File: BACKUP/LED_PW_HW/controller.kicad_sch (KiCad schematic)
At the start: 23 parts, among them SW1 SW_MEC_5E, U2 STM32L031K6Tx, Y1 Crystal

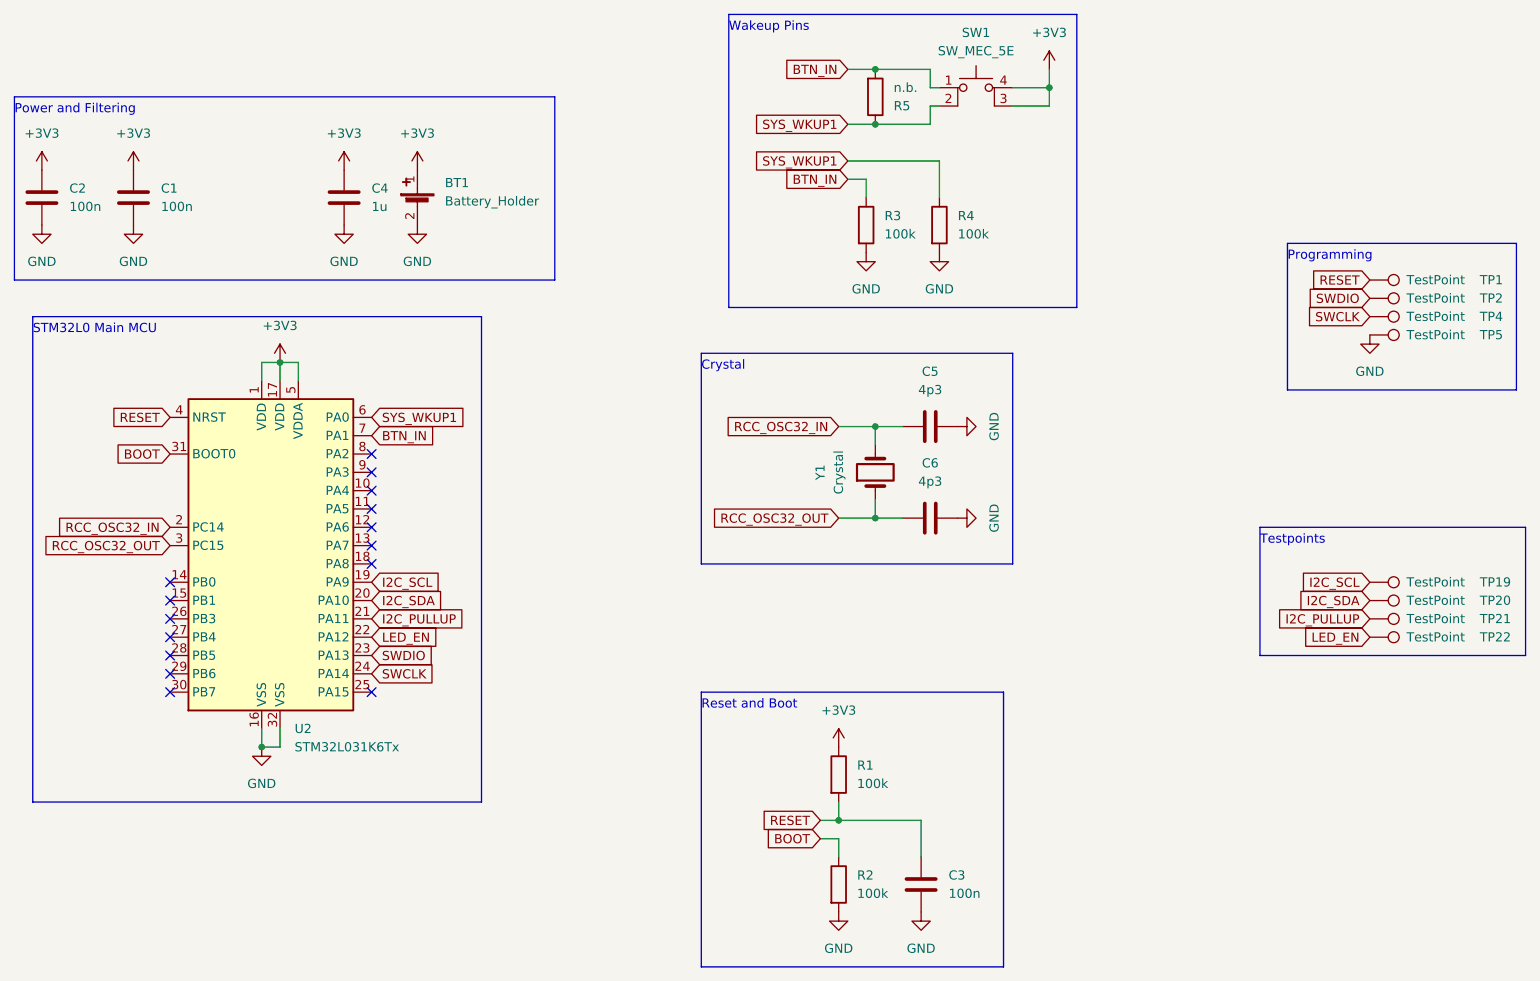
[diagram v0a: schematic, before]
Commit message: giving up for now and going with 72 leds
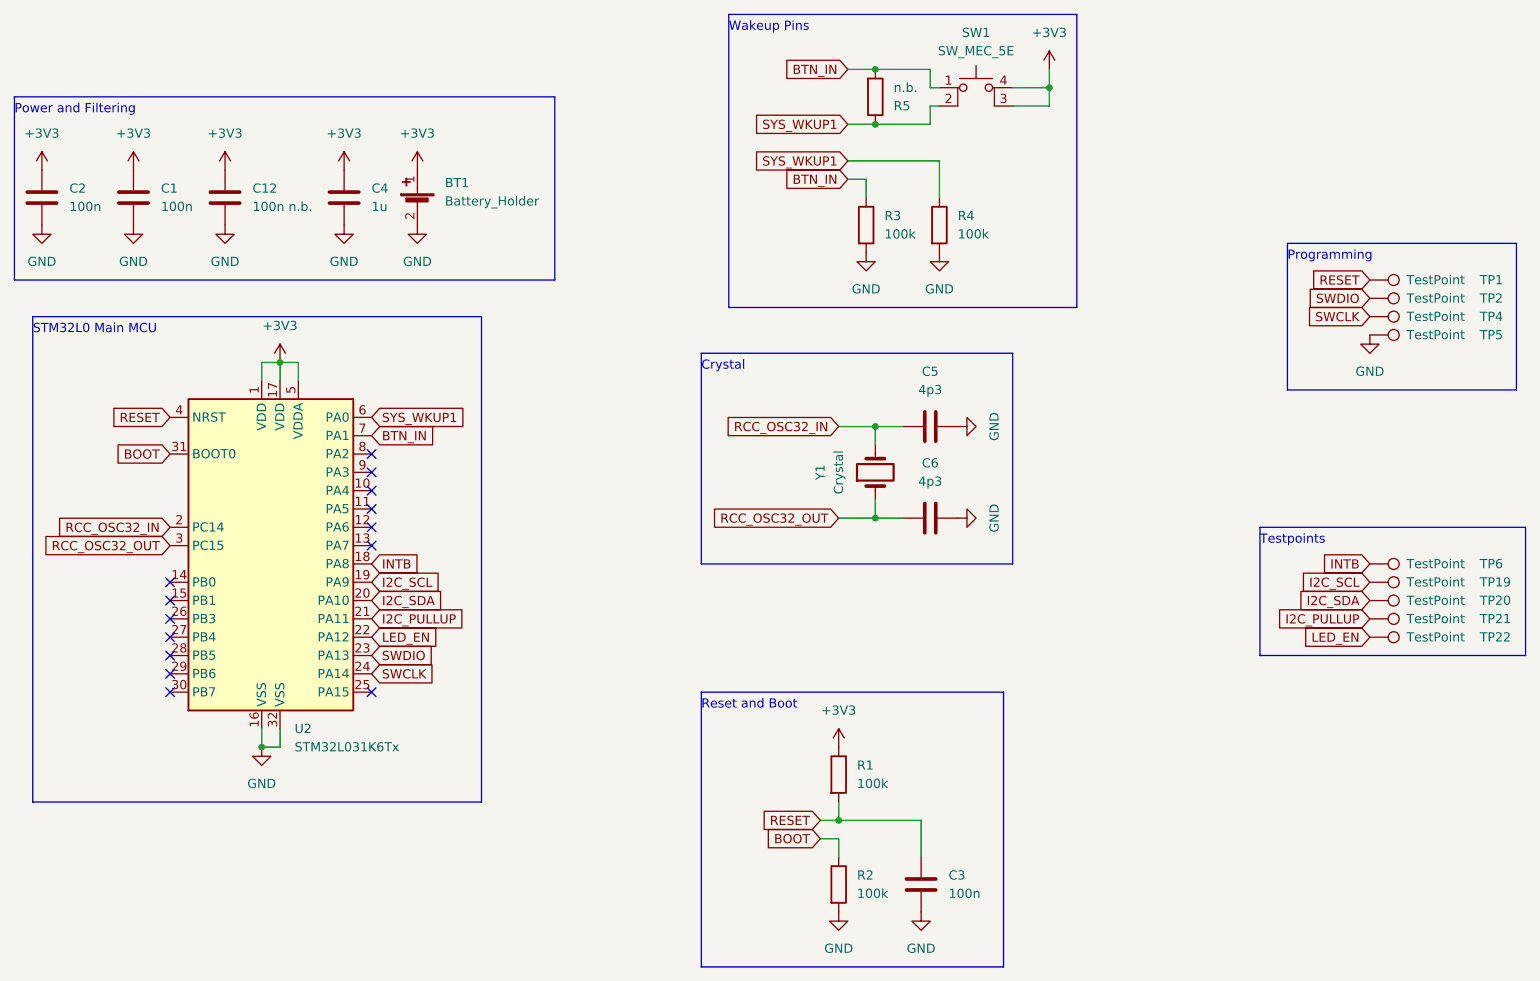
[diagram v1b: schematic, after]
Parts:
- added C12: 100n n.b., Capacitor_SMD:C_0603_1608Metric_Pad1.08x0.95mm_HandSolder, symbol Device:C
- added TP6: TestPoint, TestPoint:TestPoint_Pad_D1.5mm, symbol Connector:TestPoint
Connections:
- net +3V3: now also C12.1
- net GND: now also C12.2
- net INTB: now reaches U2.18 (PA8)
- net INTB: now also TP6.1
- no-connect marks 15 -> 14
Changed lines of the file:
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@@
   (no_connect (at 45.72 100.33))
   (no_connect (at 45.72 97.79))
-  (no_connect (at 73.66 95.25))
   (no_connect (at 73.66 92.71))
   (no_connect (at 73.66 82.55))
@@
     )
   )
+  (global_label "INTB" (shape input) (at 73.66 95.25 0) (fields_autoplaced)
+    (effects (font (size 1.27 1.27)) (justify left))
+    (property "Intersheet References" "${INTERSHEET_REFS}" (id 0) (at 80.246 95.1706 0)
+      (effects (font (size 1.27 1.27)) (justify left) hide)
+    )
+  )
   (global_label "LED_EN" (shape input) (at 73.66 105.41 0) (fields_autoplaced)
     (effects (font (size 1.27 1.27)) (justify left))
@@
     )
   )
+  (global_label "INTB" (shape input) (at 212.09 95.25 180) (fields_autoplaced)
+    (effects (font (size 1.27 1.27)) (justify right))
+    (property "Intersheet References" "${INTERSHEET_REFS}" (id 0) (at 205.504 95.3294 0)
+      (effects (font (size 1.27 1.27)) (justify right) hide)
+    )
+  )
   (global_label "SWDIO" (shape input) (at 212.09 58.42 180) (fields_autoplaced)
     (effects (font (size 1.27 1.27)) (justify right))
@@
     (pin "1")
   )
+  (symbol (lib_id "Connector:TestPoint") (at 212.09 95.25 270) (unit 1)
+    (in_bom yes) (on_board yes)
+    (property "Reference" "TP6" (id 0) (at 227.33 95.25 90)
+      (effects (font (size 1.27 1.27)) (justify left))
+    )
+    (property "Value" "TestPoint" (id 1) (at 217.17 95.25 90)
+      (effects (font (size 1.27 1.27)) (justify left))
+    )
+    (property "Footprint" "TestPoint:TestPoint_Pad_D1.5mm" (id 2) (at 212.09 100.33 0)
+      (effects (font (size 1.27 1.27)) hide)
+    )
+    (property "Datasheet" "~" (id 3) (at 212.09 100.33 0)
+      (effects (font (size 1.27 1.27)) hide)
+    )
+    (pin "1")
+  )
+  (symbol (lib_id "power:+3V3") (at 53.34 40.64 0) (unit 1)
+    (in_bom yes) (on_board yes) (fields_autoplaced)
+    (property "Reference" "#PWR0109" (id 0) (at 53.34 44.45 0)
+      (effects (font (size 1.27 1.27)) hide)
+    )
+    (property "Value" "+3V3" (id 1) (at 53.34 35.56 0))
+    (property "Footprint" "" (id 2) (at 53.34 40.64 0)
+      (effects (font (size 1.27 1.27)) hide)
+    )
+    (property "Datasheet" "" (id 3) (at 53.34 40.64 0)
+      (effects (font (size 1.27 1.27)) hide)
+    )
+    (pin "1")
+  )
   (symbol (lib_id "Connector:TestPoint") (at 212.09 60.96 270) (unit 1)
     (in_bom yes) (on_board yes)
@@
     )
     (pin "1")
+  )
+  (symbol (lib_id "Device:C") (at 53.34 44.45 0) (unit 1)
+    (in_bom yes) (on_board yes) (fields_autoplaced)
+    (property "Reference" "C12" (id 0) (at 57.15 43.1799 0)
+      (effects (font (size 1.27 1.27)) (justify left))
+    )
+    (property "Value" "100n n.b." (id 1) (at 57.15 45.7199 0)
+      (effects (font (size 1.27 1.27)) (justify left))
+    )
+    (property "Footprint" "Capacitor_SMD:C_0603_1608Metric_Pad1.08x0.95mm_HandSolder" (id 2) (at 54.3052 48.26 0)
+      (effects (font (size 1.27 1.27)) hide)
+    )
+    (property "Datasheet" "~" (id 3) (at 53.34 44.45 0)
+      (effects (font (size 1.27 1.27)) hide)
+    )
+    (pin "1")
+    (pin "2")
   )
   (symbol (lib_id "Connector:TestPoint") (at 212.09 63.5 270) (unit 1)
@@
       (effects (font (size 1.27 1.27)) hide)
     )
+    (pin "1")
+  )
+  (symbol (lib_id "power:GND") (at 53.34 48.26 0) (unit 1)
+    (in_bom yes) (on_board yes) (fields_autoplaced)
+    (property "Reference" "#PWR0110" (id 0) (at 53.34 54.61 0)
+      (effects (font (size 1.27 1.27)) hide)
+    )
+    (property "Value" "GND" (id 1) (at 53.34 53.34 0))
+    (property "Footprint" "" (id 2) (at 53.34 48.26 0)
+      (effects (font (size 1.27 1.27)) hide)
+    )
+    (property "Datasheet" "" (id 3) (at 53.34 48.26 0)
+      (effects (font (size 1.27 1.27)) hide)
+    )
